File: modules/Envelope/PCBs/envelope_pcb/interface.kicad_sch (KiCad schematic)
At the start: 25 parts, among them J1 THONKICONN, J2 THONKICONN, J3 THONKICONN, J4 THONKICONN, J5 THONKICONN, J6 THONKICONN, J7 THONKICONN, J8 THONKICONN, SW1 TL1105SPF250Q

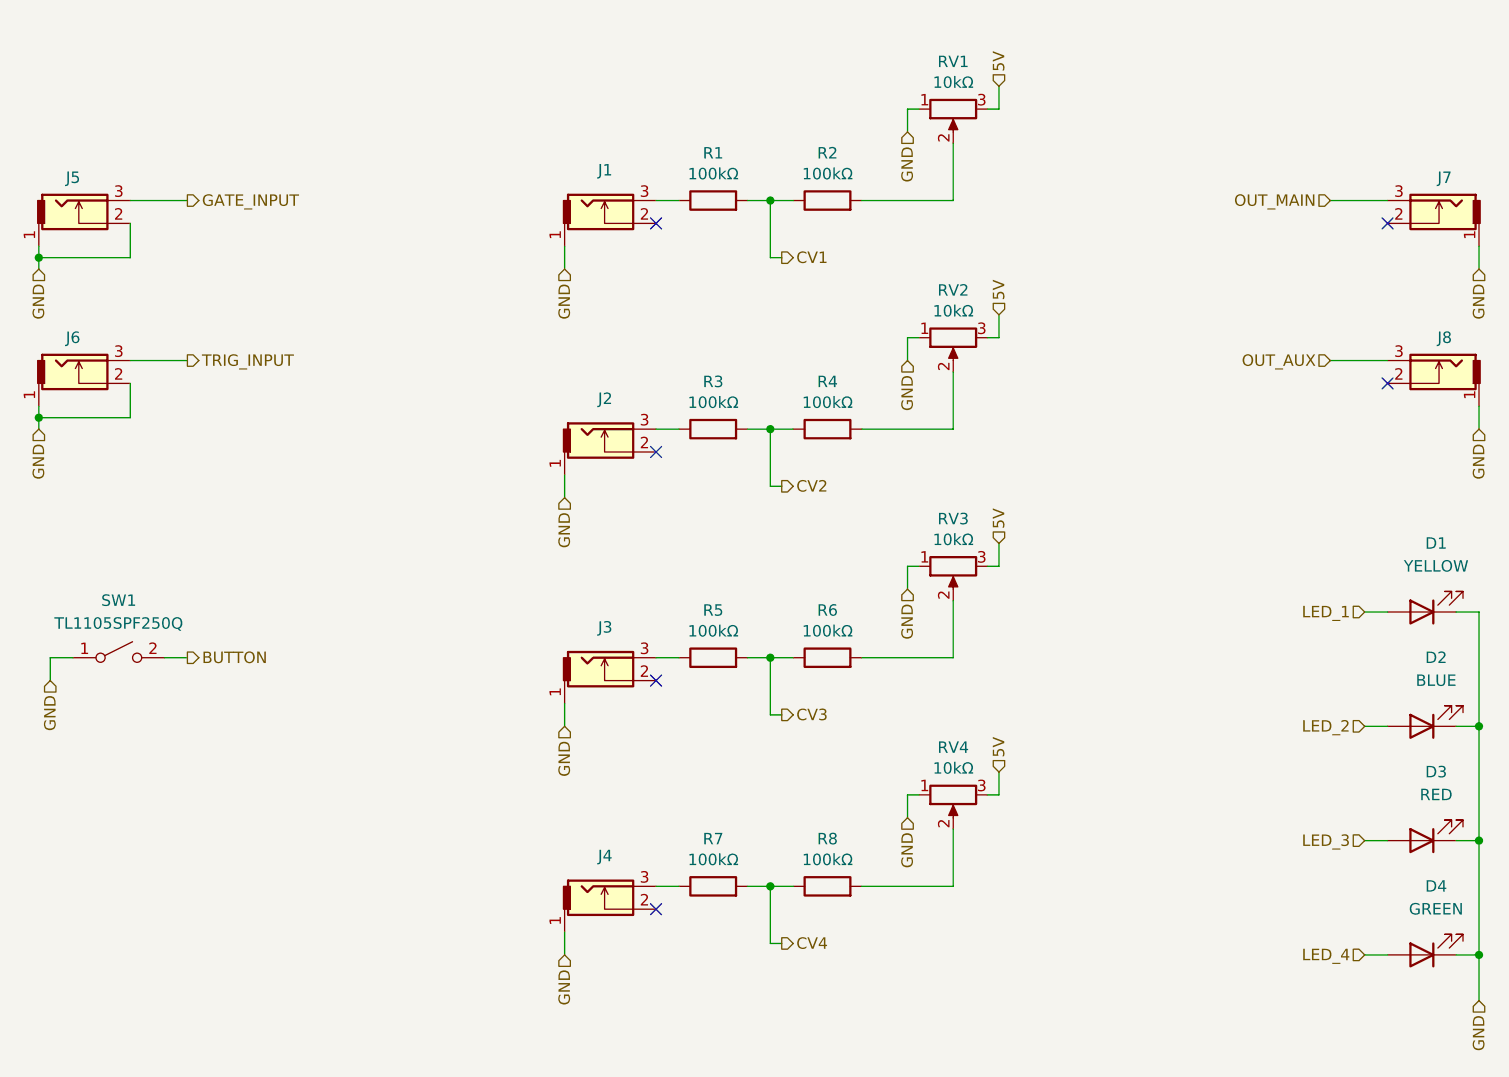
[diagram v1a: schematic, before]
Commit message: fix gate inputs for envelope
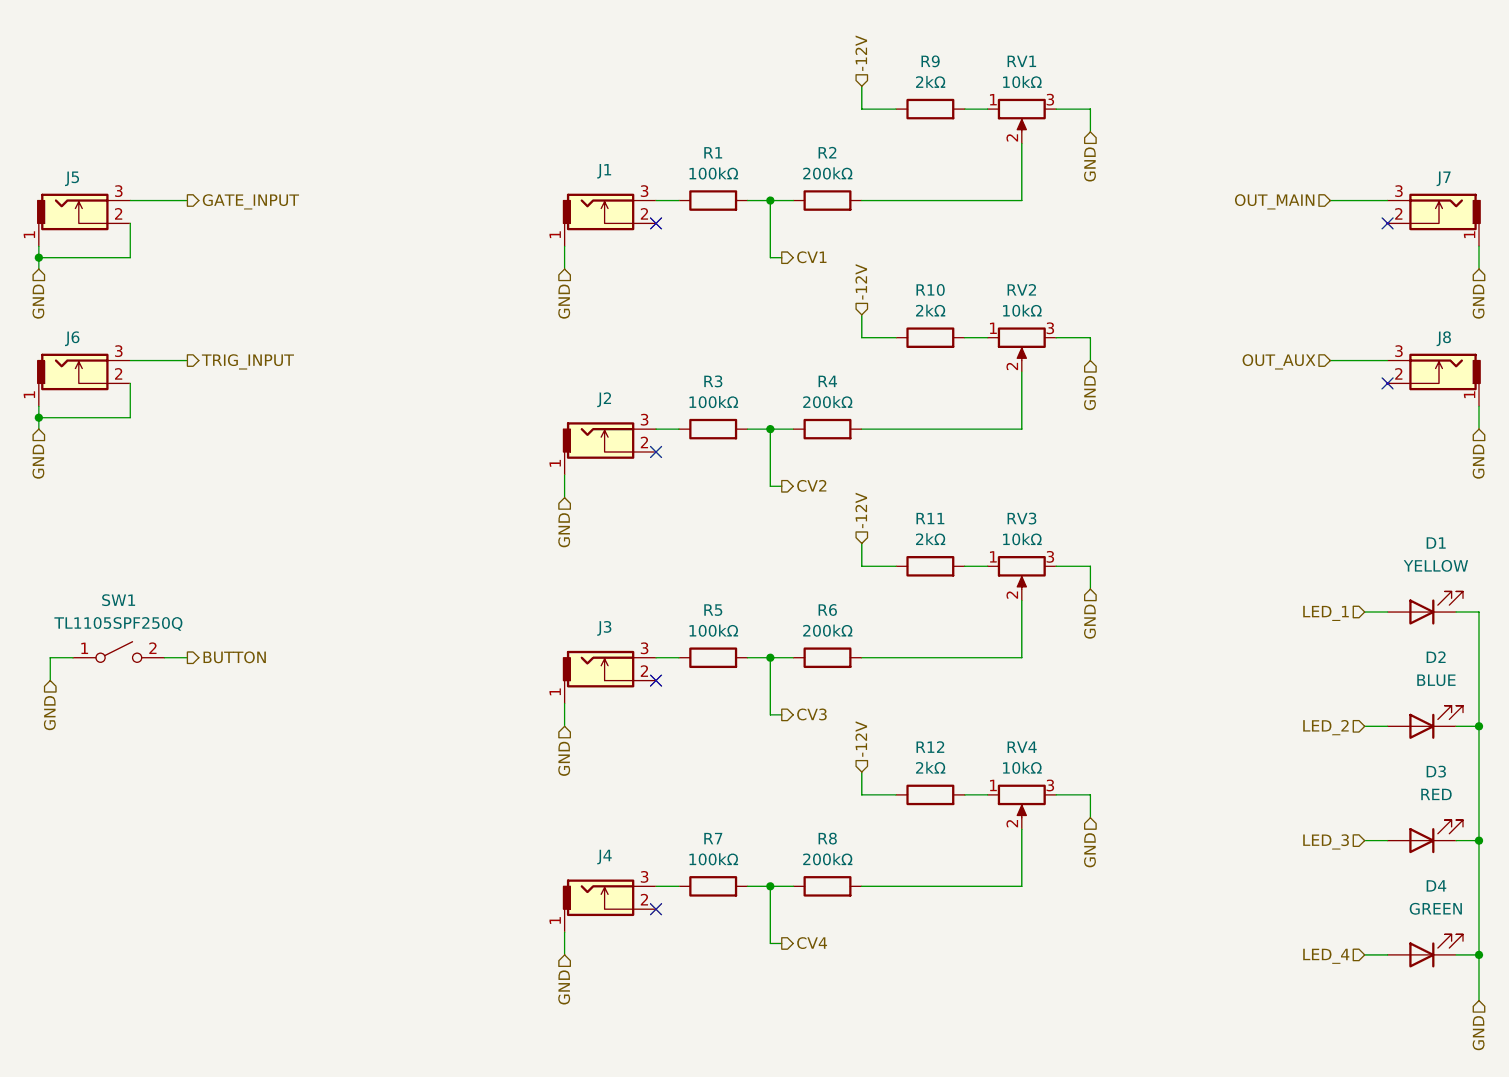
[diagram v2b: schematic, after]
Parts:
- added R10, R11, R12, R9: 2kΩ, Resistor_THT:R_Axial_DIN0207_L6.3mm_D2.5mm_P10.16mm_Horizontal, symbol Device:R
- R2, R4, R6, R8: value 100kΩ -> 200kΩ
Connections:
- net 5V is gone; now on net GND: RV1.3, RV2.3, RV3.3, RV4.3
- net GND: no longer RV1.1, RV2.1, RV3.1, RV4.1
- new net: R9.2, RV1.1
- new net: R10.2, RV2.1
- new net: R11.2, RV3.1
- new net: R12.2, RV4.1
- new net -12V: R10.1, R11.1, R12.1, R9.1
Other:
- moved on the sheet: RV1, RV2, RV3, RV4
